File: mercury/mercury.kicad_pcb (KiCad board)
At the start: 2 copper layers, 111.3 x 99.9 mm, 137 parts, among them IC1 AS5600-ML, IC2 AS5600-MR, J1 Battery, J2 UART, J3 USB_C_Receptacle_USB2.0, J4 Conn_01x02_Socket, J5 Conn_01x02_Socket, J6 Encoder_L, J7 Encoder_R, Q1 NMOS, Q10 SR_RECV, Q11 SL_RECV, Q12 NMOS, Q2 NMOS, Q3 NMOS, Q4 FR_RECV, Q5 FL_RECV, Q6 R_RECV, Q7 L_RECV, Q8 NMOS, Q9 NMOS, SW1 SW_Push, SW2 SW_Push, SW3 SW_Push, SW4 SW_Push, U1 ZXMHC3F381N8TC, U10 MPU-6500, U12 LMZ10501SILR, U2 UCC27524ADR, U3 UCC27524ADR, U4 ZXMHC3F381N8TC, U5 MCP1700, U6 TPS73633DBV, U8 LM1085-5.0, U9 ESP32-S3-WROOM-1U-N16R8

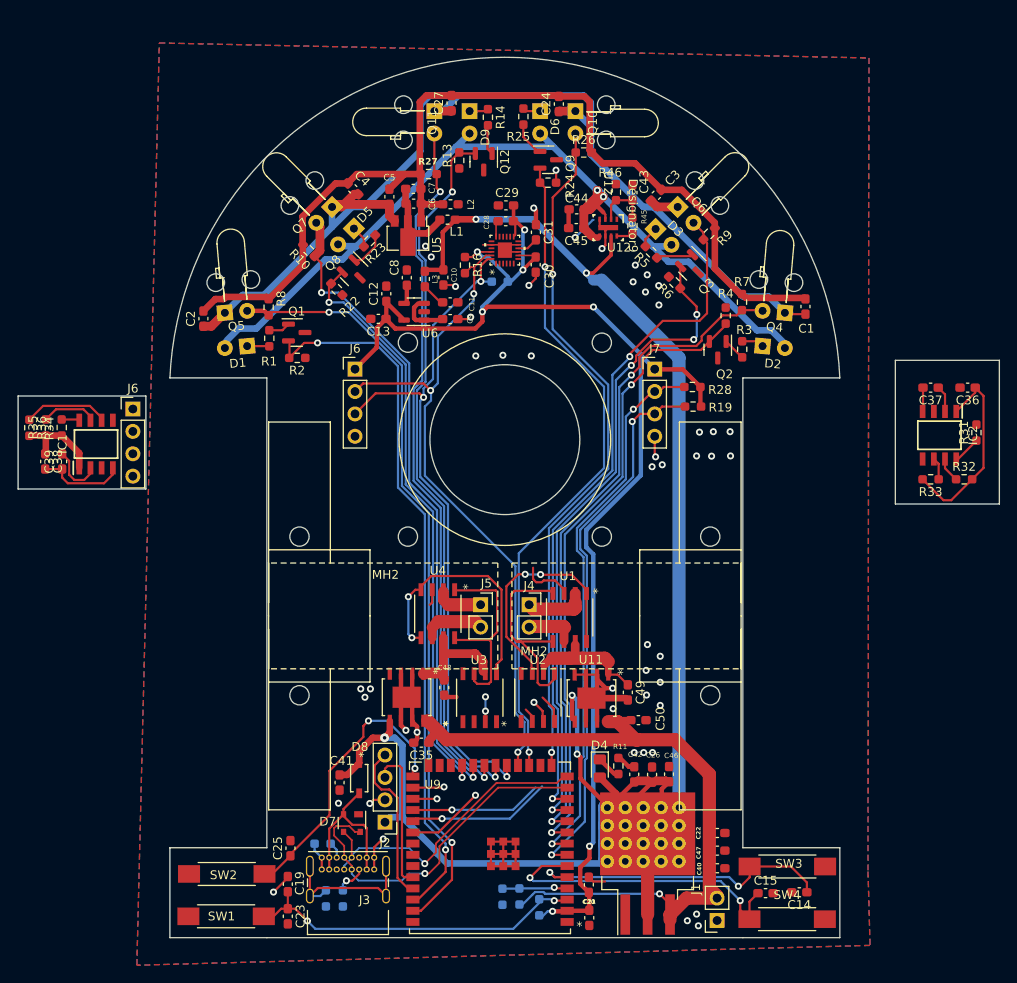
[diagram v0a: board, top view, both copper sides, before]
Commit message: completed 4 sensor pcb
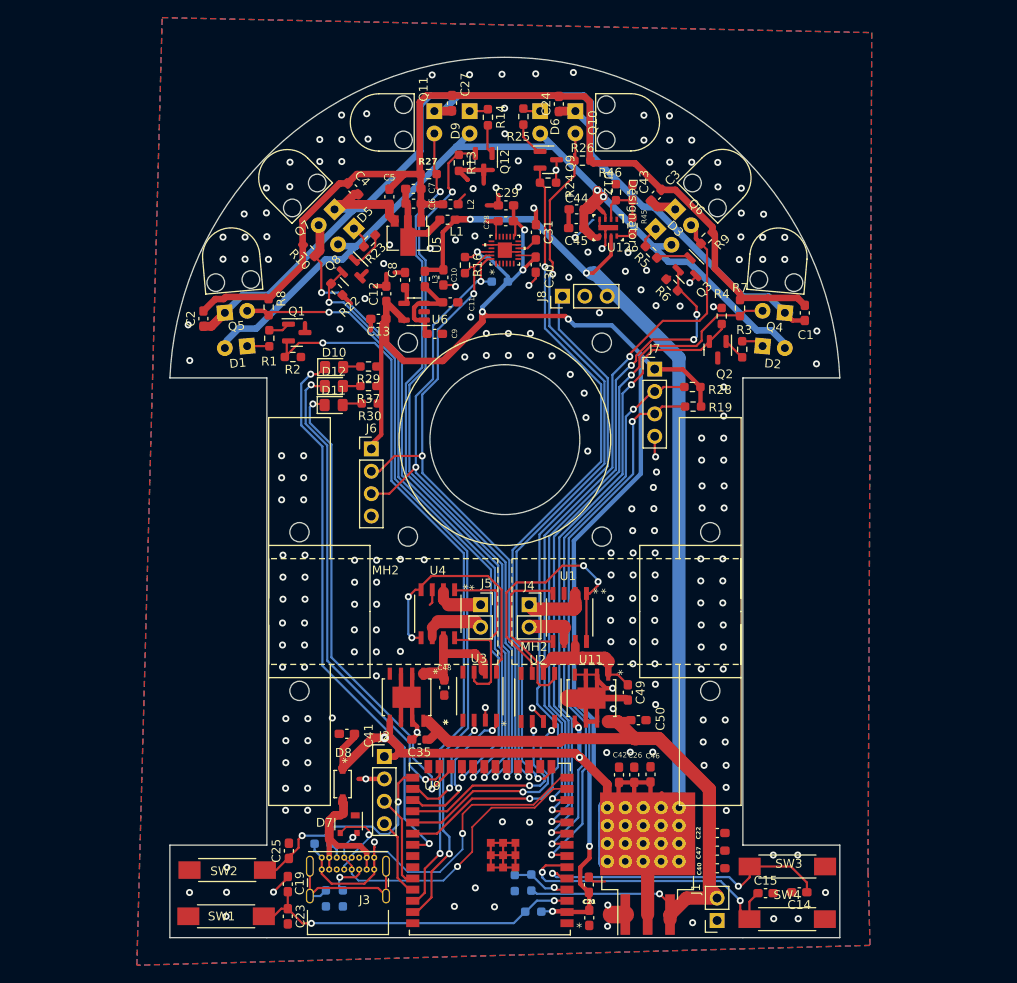
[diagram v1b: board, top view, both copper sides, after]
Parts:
- removed C36, C38: 100nF, Capacitor_SMD:C_0603_1608Metric_Pad1.08x0.95mm_HandSolder
- removed C37, C39: 1uF, Capacitor_SMD:C_0603_1608Metric_Pad1.08x0.95mm_HandSolder
- removed D4: LED, LED_SMD:LED_0805_2012Metric_Pad1.15x1.40mm_HandSolder
- removed IC1: AS5600-ML, footprint:SOIC127P600X175-8N
- removed IC2: AS5600-MR, footprint:SOIC127P600X175-8N
- removed the J6 at (84.8, 98.5)
- removed R11: R_US, Resistor_SMD:R_0603_1608Metric_Pad0.98x0.95mm_HandSolder
- removed R31, R32, R33, R34, R35, R36: 4.7k, Resistor_SMD:R_0603_1608Metric_Pad0.98x0.95mm_HandSolder
- added D10: GREEN_LED, LED_SMD:LED_0805_2012Metric_Pad1.15x1.40mm_HandSolder, F.Cu at (107.6, 93.8)
- added D11: RED_LED, LED_SMD:LED_0805_2012Metric_Pad1.15x1.40mm_HandSolder, F.Cu at (107.6, 98.1)
- added D12: BLUE_LED, LED_SMD:LED_0805_2012Metric_Pad1.15x1.40mm_HandSolder, F.Cu at (107.6, 95.9)
- added J8: Conn_01x03_Socket, Connector_PinHeader_2.54mm:PinHeader_1x03_P2.54mm_Vertical, F.Cu at (133.5, 85.7)
- added R29: 75, Resistor_SMD:R_0603_1608Metric_Pad0.98x0.95mm_HandSolder, F.Cu at (111.5, 93.7)
- added R30: 750, Resistor_SMD:R_0603_1608Metric_Pad0.98x0.95mm_HandSolder, F.Cu at (111.7, 97.9)
- added R37: 75, Resistor_SMD:R_0603_1608Metric_Pad0.98x0.95mm_HandSolder, F.Cu at (111.5, 95.9)
- C1: value 1uF -> 2.2uF
- moved J6 9.24 mm to (111.8, 103.0)
- moved J2 7.45 mm to (113.3, 137.9), turned to 0 degrees
- moved C41 5.59 mm to (109.1, 135.4), turned to 180 degrees
- moved C9 2.42 mm to (119.0, 90.0)
- moved C46 2.10 mm to (143.5, 140.0)
- moved R21 2.09 mm to (128.1, 152.3)
- moved R20 2.07 mm to (130.0, 152.2)
- moved C26 2.03 mm to (141.7, 140.0)
- moved D8 1.99 mm to (108.6, 141.1)
- moved C42 1.73 mm to (139.9, 140.0)
- moved R26 0.94 mm to (135.8, 70.3)
- moved R12 0.84 mm to (130.2, 155.6), turned to 180 degrees
- moved C1 0.73 mm to (161.0, 87.6)
- moved R7 0.71 mm to (153.7, 87.1)
- moved R9 0.55 mm to (149.9, 79.1)
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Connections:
- U9 pad 24: unconnected-(U9-IO47-Pad24) -> /RED_LED
- U9 pad 25: unconnected-(U9-IO48-Pad25) -> /BLUE_LED
- U9 pad 33: unconnected-(U9-IO40-Pad33) -> /GREEN_LED
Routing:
- net /FAN_PWM: track 8.86 -> 80.8 mm
- net /GREEN_LED: track 0.00 -> 63.6 mm, vias 0 -> 2
- net /BLUE_LED: track 0.00 -> 55.2 mm, vias 0 -> 2
- net /RED_LED: track 0.00 -> 54.3 mm, vias 0 -> 2
- net /5V: track 289.9 -> 241.0 mm
- net 3.3V: track 158.9 -> 174.0 mm
- net /ML_PWMB: track 2.74 -> 16.9 mm, vias 1 -> 2
- net /SDA_1: track 89.1 -> 76.2 mm
- net GND: track 125.5 -> 138.0 mm, vias 53 -> 215
- net /ML_PWMA: track 3.96 -> 14.0 mm, vias 1 -> 2
- net /UART_TX: track 19.0 -> 9.05 mm
- net /BOOT: track 32.6 -> 25.3 mm
- net /MR_PWMA: track 16.6 -> 23.7 mm, vias 1 -> 2
- net /SR_RECV: track 78.7 -> 85.7 mm
- net Net-(IC1-VDD3V3): track 6.74 -> 0.00 mm
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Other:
- board size 111.3 x 99.9 mm -> 76 x 99.9 mm
- board text added: "Mercury_V1 By: Kyle Tyni 2024"
